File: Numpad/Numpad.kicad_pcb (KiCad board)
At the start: 2 copper layers, 85 parts, among them SW1 SW_Push, U1 ATmega32U4-AU, Y1 16MHz

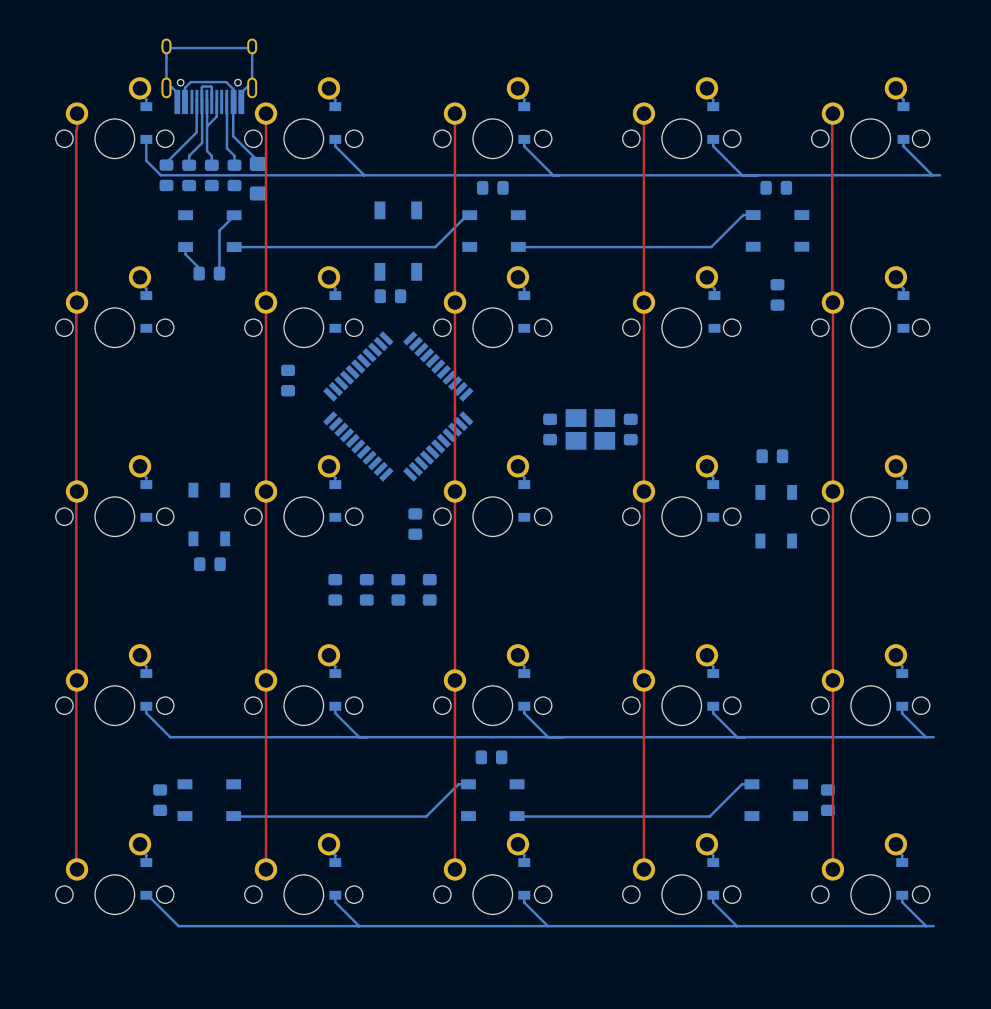
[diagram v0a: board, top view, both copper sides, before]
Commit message: finished pcb routing
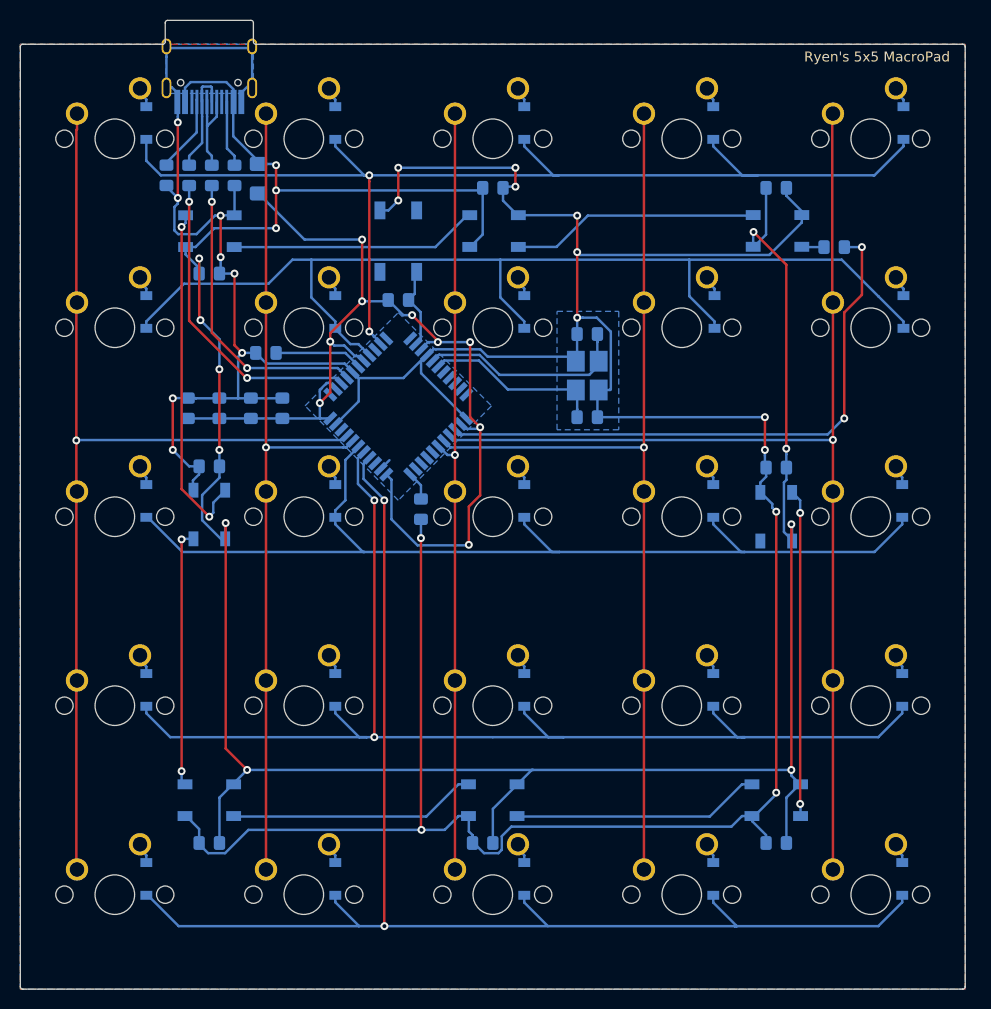
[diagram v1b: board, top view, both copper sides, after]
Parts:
- moved C7 30.5 mm to (61.2, 75.8), turned to 90 degrees
- moved C6 25.7 mm to (64.4, 75.8), turned to 90 degrees
- moved C5 21.7 mm to (67.6, 75.8), turned to 90 degrees
- moved C4 19.1 mm to (70.7, 75.8), turned to 90 degrees
- moved C2 10.3 mm to (101.5, 68.3), turned to 180 degrees
- moved C11 9.87 mm to (63.4, 81.7)
- moved C13 8.68 mm to (90.9, 119.6)
- moved R7 7.47 mm to (126.4, 59.6), turned to 180 degrees
- moved C14 6.76 mm to (120.5, 119.6), turned to 0 degrees
- moved C12 6.57 mm to (63.4, 119.6), turned to 0 degrees
- moved Y1 5.44 mm to (101.5, 72.5), turned to 90 degrees
- moved C1 4.55 mm to (101.5, 76.7), turned to 0 degrees
- moved C3 3.57 mm to (69.1, 70.2), turned to 180 degrees
- moved R4 1.61 mm to (84.7, 86.0)
- moved C15 1.21 mm to (120.5, 81.8)
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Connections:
- U1 pad 10: Net-(U1-Pad10) -> ROW0
- U1 pad 25: Net-(U1-Pad25) -> LED
- U1 pad 26: Net-(U1-Pad26) -> COL4
- U1 pad 27: Net-(U1-Pad27) -> COL3
- U1 pad 28: Net-(U1-Pad28) -> COL2
- U1 pad 37: Net-(U1-Pad37) -> ROW4
- U1 pad 38: Net-(U1-Pad38) -> ROW3
- U1 pad 39: Net-(U1-Pad39) -> ROW2
- U1 pad 40: Net-(U1-Pad40) -> COL1
- U1 pad 41: Net-(U1-Pad41) -> COL0
- U1 pad 8: Net-(U1-Pad8) -> ROW1
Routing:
- net GND: track 28.1 -> 386.0 mm, vias 0 -> 21
- net VCC: track 18.8 -> 272.2 mm, vias 0 -> 13
- net ROW1: track 0.00 -> 111.2 mm
- net +5V: track 0.00 -> 105.6 mm, vias 0 -> 9
- net ROW2: track 0.00 -> 102.7 mm
- net LED: track 0.00 -> 59.9 mm, vias 0 -> 2
- net ROW4: track 97.1 -> 140.1 mm, vias 0 -> 2
- net COL4: track 75.7 -> 114.5 mm, vias 0 -> 1
- net Net-(LED2-Pad2): track 0.00 -> 35.2 mm, vias 0 -> 2
- net Net-(LED6-Pad2): track 0.00 -> 32.9 mm, vias 0 -> 2
- net Net-(R3-Pad1): track 0.00 -> 31.6 mm, vias 0 -> 2
- net Net-(R2-Pad1): track 0.00 -> 30.3 mm, vias 0 -> 2
- net COL0: track 76.3 -> 103.8 mm, vias 0 -> 1
- net Net-(LED3-Pad2): track 0.00 -> 26.1 mm, vias 0 -> 2
- net ROW3: track 100.6 -> 124.9 mm, vias 0 -> 2
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- added copper zone on B.Cu, net GND
- added copper zone on F.Cu, net GND
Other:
- board outline added: 95.2 x 97.7 mm
- board text added: "Ryen's 5x5 MacroPad"
